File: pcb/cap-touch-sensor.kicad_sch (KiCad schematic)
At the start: 6 parts, among them U4 CAP1296-x-AIA

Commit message: Replaced through-hole components with SMD
- Other small edits (e.g. optional jumper to force USB-boot)
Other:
- company: (none) -> Open Ephys, Inc.
- title: (none) -> Open Ephys Commutator Controller
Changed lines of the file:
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@@
 	(generator_version "8.0")
 	(paper "A5")
+	(title_block
+		(title "Open Ephys Commutator Controller")
+		(rev "D")
+		(company "Open Ephys, Inc.")
+	)
 	(junction
 		(at 101.6 46.99)

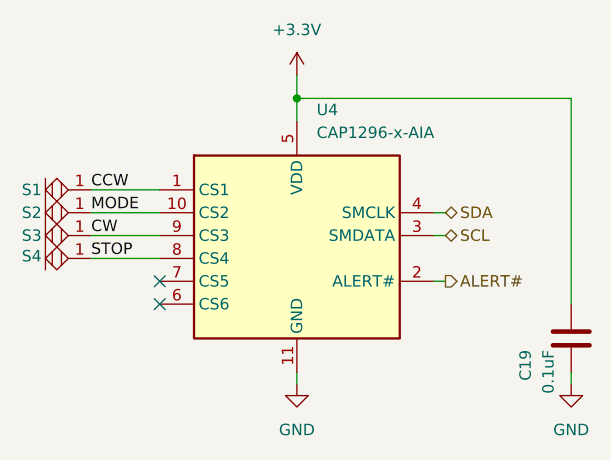
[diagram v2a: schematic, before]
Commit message: Rev D PCB WIP for Review
- Before going into further minutiae, get review
- Components are laid out and routed
- Fails DRC check, requires vias for better GND plane, there are traces
  in the outer keepout zone, remove S5?
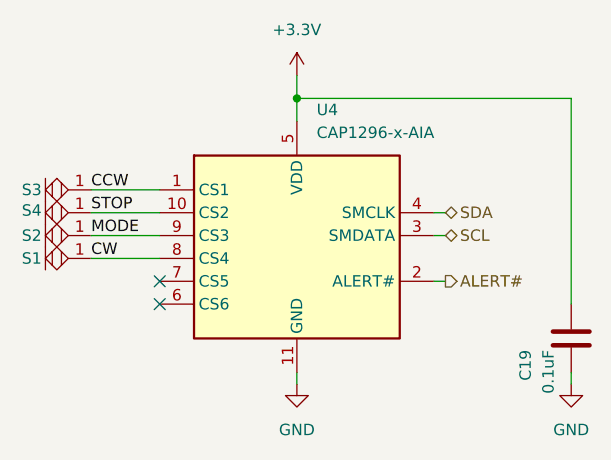
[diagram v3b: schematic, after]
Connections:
- net CCW: now also S3.1; no longer S1.1
- net CW: now also S1.1, U4.8 (CS4); no longer S3.1, U4.9 (CS3)
- net MODE: now also U4.9 (CS3); no longer U4.10 (CS2)
- net STOP: now also U4.10 (CS2); no longer U4.8 (CS4)
